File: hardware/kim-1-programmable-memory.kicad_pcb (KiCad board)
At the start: 4 copper layers, 107.5 x 75.4 mm, 45 parts, among them J1 Conn_02x01, J2 EDGE_CONN, J3 VGA, J4 VIdeo Out, J5 Micro_SD_Card_Det1, Q1 DMG2305UX, SW1 RESET, U1 LVC04, U2 74LVC1G38, U3 74LVC541, U4 74LVC541, U5 74LVC245, U6 74LVC1G27, U7 LVC04, U8 PicoW

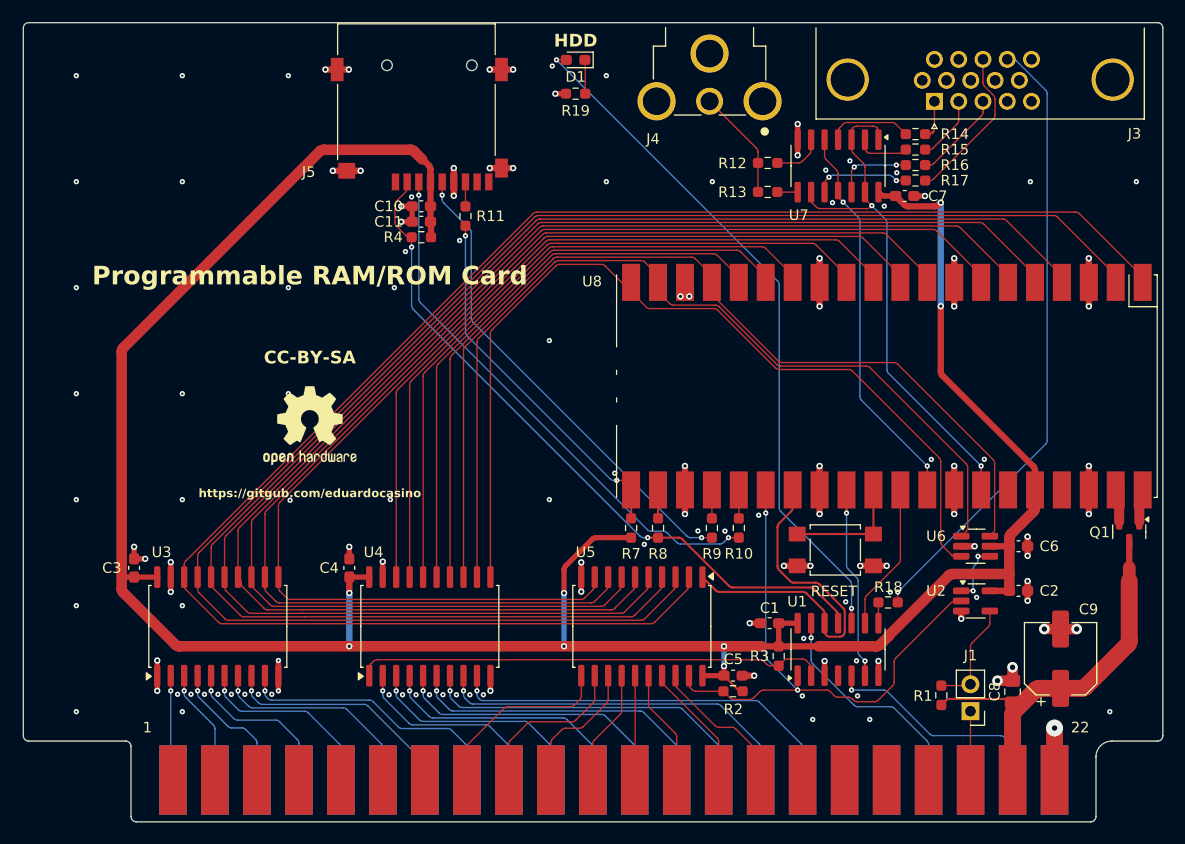
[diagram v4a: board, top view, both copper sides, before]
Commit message: Minor silkscreen changes, track width corrections, open hole for Pico antenna
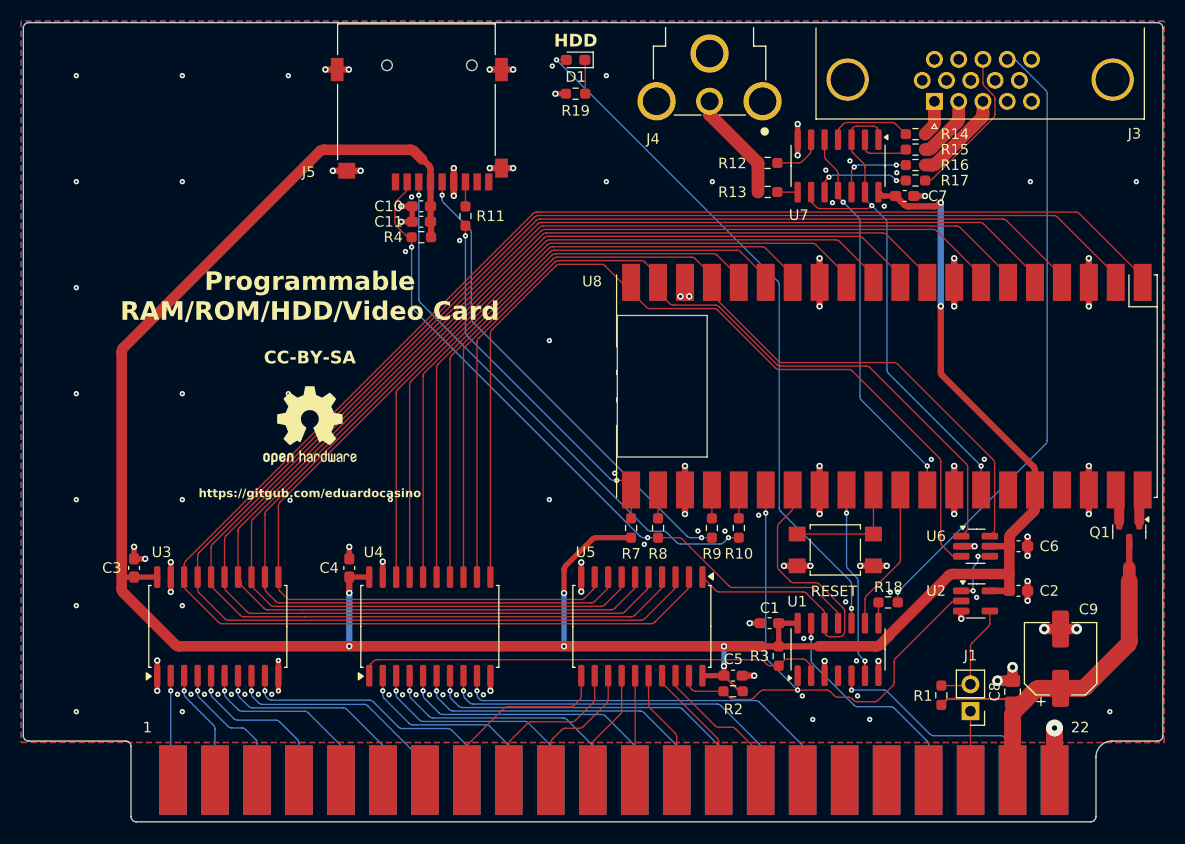
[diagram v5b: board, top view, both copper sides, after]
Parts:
- J2: footprint MTU_Library:EDGE_CONN -> MTU:EDGE_CONN
- R10, R11, R8, R9: value 40R -> 47R
- U7: footprint Package_SO:SOIC-14_3.9x8.7mm_P1.27mm -> SOIC:SOIC-14_3.9x8.7mm_P1.27mm
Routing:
- added copper zone on B.Cu, net GND
- added copper zone on F.Cu, net GND
- removed copper zone on In1.Cu, net GND
- removed copper zone on In2.Cu, net GND
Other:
- outline, holes or cut-outs redrawn
- copper layers 4 -> 2
- board text added: "Programmable RAM/ROM/HDD/Video Card"
- board text removed: "Programmable RAM/ROM Card"

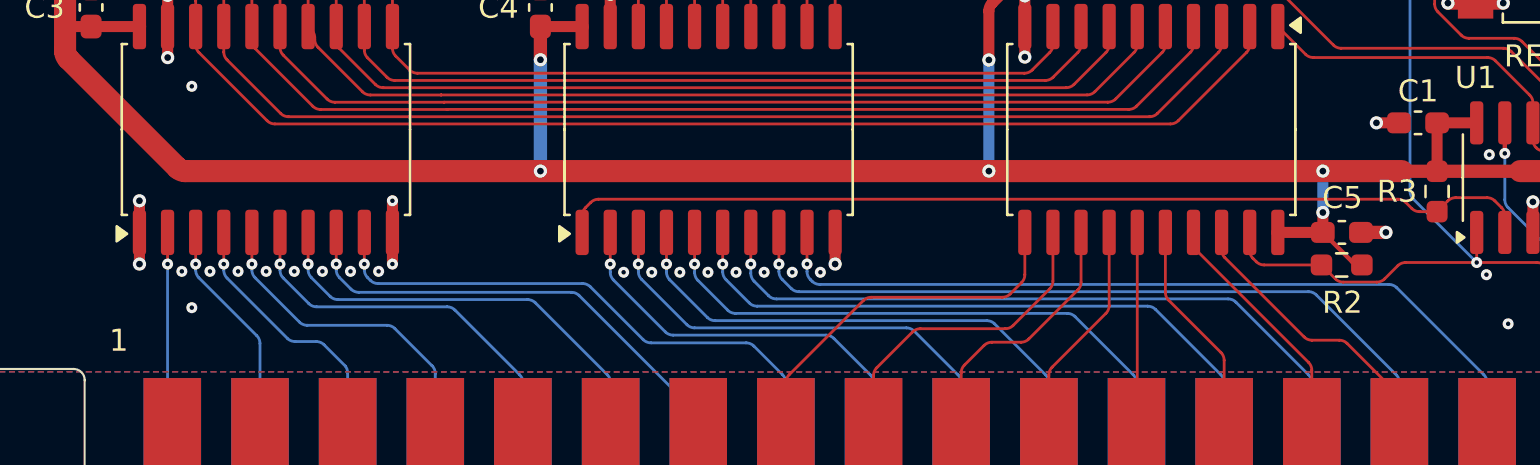
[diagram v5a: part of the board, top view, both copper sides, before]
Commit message: New design: bus multiplexing and video and sd card support
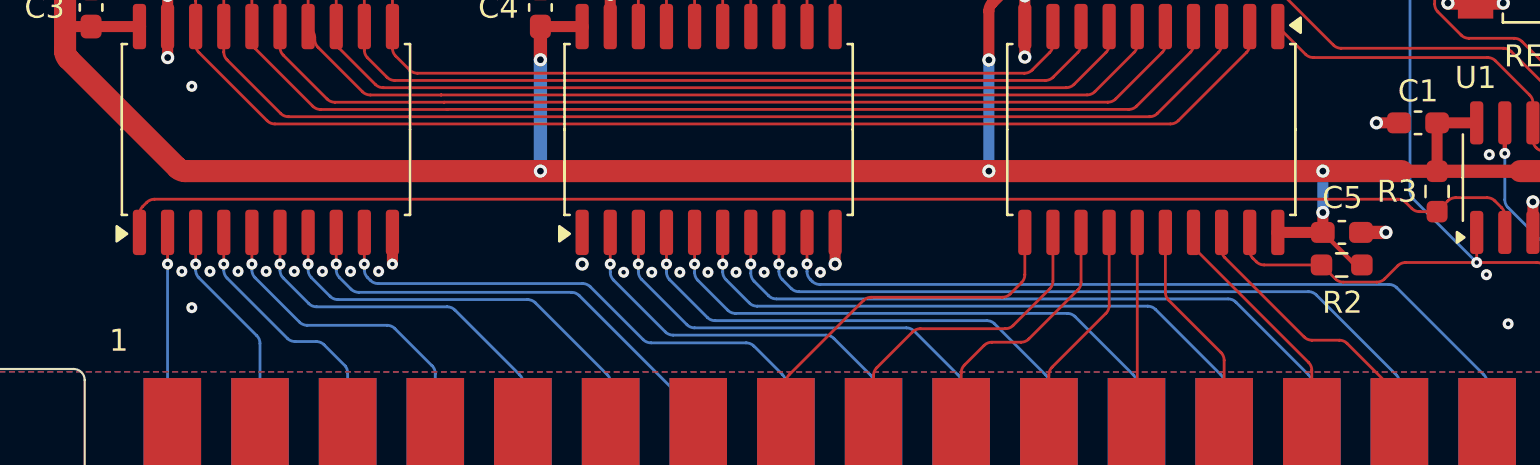
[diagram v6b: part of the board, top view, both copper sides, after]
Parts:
- R19: value 100R -> 150R
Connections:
- R3 pad 1: Net-(U4-G1) -> Net-(U3-G1)
- U1 pad 2: Net-(U4-G1) -> Net-(U3-G1)
- U3 pad 1: GND -> Net-(U3-G1)
- U4 pad 1: Net-(U4-G1) -> GND
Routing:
- net Net-(U3-G1): track 0.00 -> 64.5 mm
- net Net-(U4-G1): track 44.4 -> 0.00 mm
- net GND: track 95.8 -> 92.3 mm, vias 132 -> 130

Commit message: Silly silkscreen mistake
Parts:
- D1: value HDD -> FDC
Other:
- board text added: "Programmable RAM/ROM/FDD/Video Card"
- board text removed: "Programmable RAM/ROM/HDD/Video Card"
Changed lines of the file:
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@@
         (effects (font (size 1 1) (thickness 0.15)))
     )
-    (fp_text value "HDD" (at -0.01 1.816) (layer "F.SilkS")
+    (fp_text value "FDC" (at -0.01 1.816) (layer "F.SilkS")
         (effects (font (size 1.2 1.2) (thickness 0.2) bold))
     )
@@
       (rotate (xyz 0 0 0))
     )
+    (model "${KIPRJMOD}/3dmodels/Jumper-green.step"
+      (offset (xyz 0 -1.27 0.2))
+      (scale (xyz 1 1 1))
+      (rotate (xyz 0 0 90))
+    )
   )
   (footprint "Capacitor_SMD:C_0603_1608Metric_Pad1.08x0.95mm_HandSolder" (layer "F.Cu")
@@
     (effects (font (size 1.2 1.2) (thickness 0.2) bold) (justify bottom))
   )
-  (gr_text "Programmable\nRAM/ROM/HDD/Video Card" (at 78.33 116.67) (layer "F.SilkS" knockout)
+  (gr_text "Programmable\nRAM/ROM/FDD/Video Card" (at 78.33 116.67) (layer "F.SilkS" knockout)
     (effects (font (size 1.75 1.75) (thickness 0.3) bold) (justify bottom))
   )
